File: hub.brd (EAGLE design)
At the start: 64.1 x 51.7 mm, 50 parts, among them IC1 SN65220DBV, IC2 SN65220DBV, IC3 SN65220DBV, IC4 SN65220DBV, IC5 SN65220DBV, U1 LM3526-L, X1 12MHz

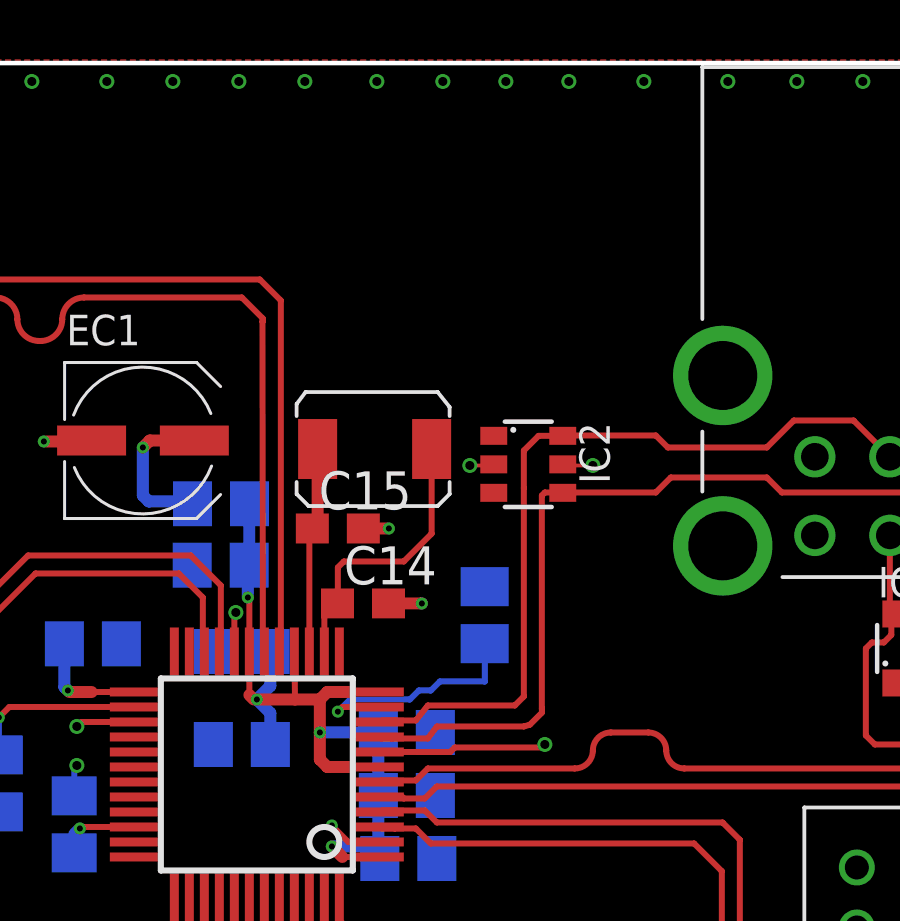
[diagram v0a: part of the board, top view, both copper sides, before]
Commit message: switch to crystal with correct drive level (supporting 600μW)
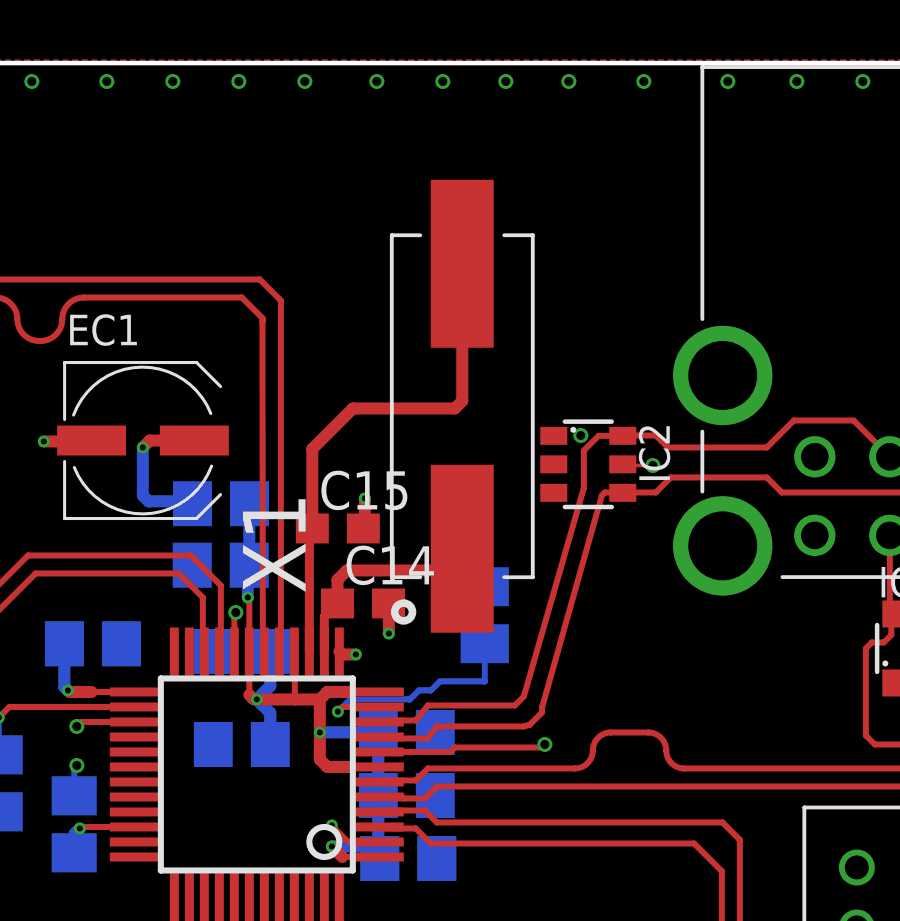
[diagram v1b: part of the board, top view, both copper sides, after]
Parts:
- X1: device Ava:ABRACON_ABM3_CRYSTAL -> ABLS-12.000MHZ-B2-T:XTAL_ABLS2-24.000MHZ-D4YF-T
- moved X1 4.62 mm to (39.0, 40.3), turned to 90 degrees
- moved IC2 2.00 mm to (43.2, 38.3)
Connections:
- net XIN: now also X1.1; no longer X1.P$1
- net XOUT: now also X1.2; no longer X1.P$2
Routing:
- net XOUT: track 6.86 -> 17.0 mm
- net XIN: track 9.40 -> 7.16 mm
- net D2_N: track 28.1 -> 26.4 mm
- net D2_P: track 27.5 -> 25.8 mm
- net GND: track 49.6 -> 49.5 mm, vias 122 -> 123

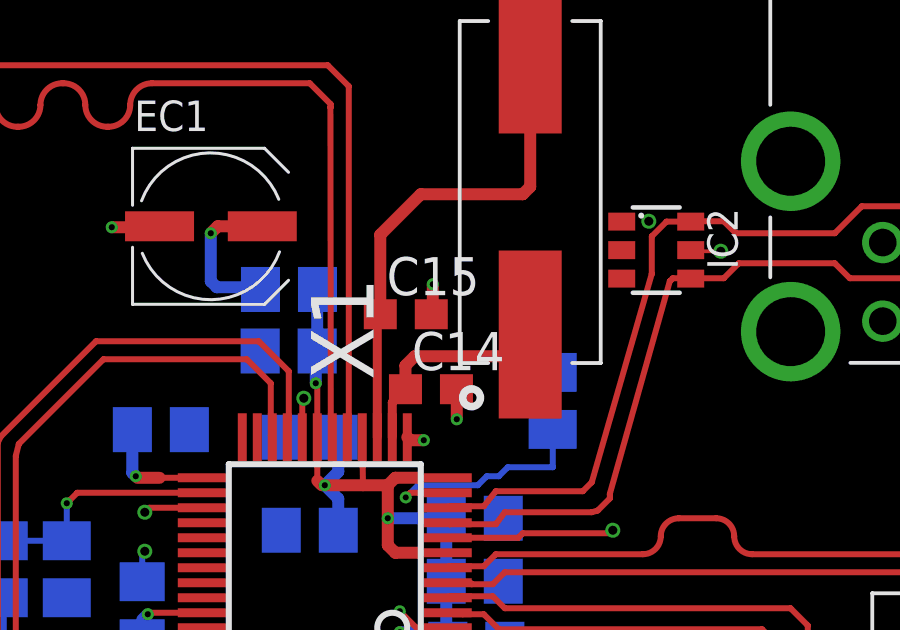
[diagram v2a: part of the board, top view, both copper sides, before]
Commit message: Switch to 0805 capacitors for consistency
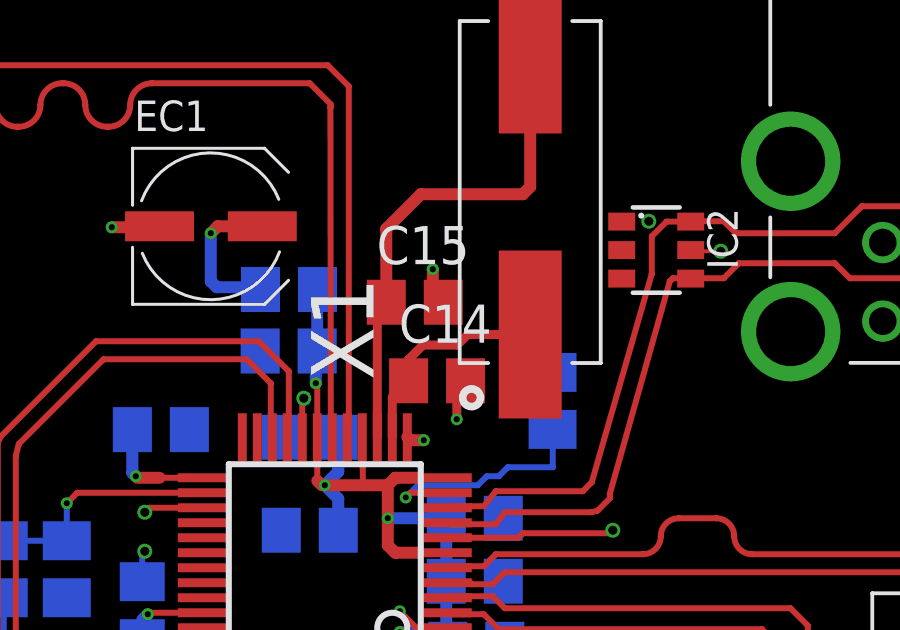
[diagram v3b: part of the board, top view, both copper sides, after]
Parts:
- C14, C15: device rcl:C0603 -> rcl:C0805
- moved C15 0.50 mm to (35.2, 36.6)
- moved C14 0.35 mm to (35.9, 34.0)
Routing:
- net GND: track 49.5 -> 50.1 mm
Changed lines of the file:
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@@
 <element name="R2" library="rcl" library_urn="urn:adsk.eagle:library:334" package="M0805" package3d_urn="urn:adsk.eagle:package:23556/1" value="100K" x="28.064" y="19.216" rot="MR0"/>
 <element name="R3" library="rcl" library_urn="urn:adsk.eagle:library:334" package="M0805" package3d_urn="urn:adsk.eagle:package:23556/1" value="650R 1%" x="39.794" y="33.31" rot="MR270"/>
-<element name="C14" library="rcl" library_urn="urn:adsk.eagle:library:334" package="C0603" package3d_urn="urn:adsk.eagle:package:23616/2" value="18P" x="35.739" y="33.702">
-<attribute name="DIGIKEY" value="1276-1089-1-ND" x="35.739" y="33.702" size="1.778" layer="27" display="off"/>
-<attribute name="OC_MOUSER" value="77-VJ0603A180JXACBC" x="35.739" y="33.702" size="1.778" layer="27" display="off"/>
-</element>
-<element name="C15" library="rcl" library_urn="urn:adsk.eagle:library:334" package="C0603" package3d_urn="urn:adsk.eagle:package:23616/2" value="18P" x="34.9" y="36.2">
-<attribute name="DIGIKEY" value="1276-1089-1-ND" x="34.9" y="36.2" size="1.778" layer="27" display="off"/>
-<attribute name="OC_MOUSER" value="77-VJ0603A180JXACBC" x="34.9" y="36.2" size="1.778" layer="27" display="off"/>
+<element name="C14" library="rcl" library_urn="urn:adsk.eagle:library:334" package="C0805" package3d_urn="urn:adsk.eagle:package:23617/2" value="18P" x="35.943" y="33.982">
+<attribute name="DIGIKEY" value="1276-1089-1-ND" x="35.943" y="33.982" size="1.778" layer="27" display="off"/>
+<attribute name="OC_MOUSER" value="77-VJ0603A180JXACBC" x="35.943" y="33.982" size="1.778" layer="27" display="off"/>
+</element>
+<element name="C15" library="rcl" library_urn="urn:adsk.eagle:library:334" package="C0805" package3d_urn="urn:adsk.eagle:package:23617/2" value="18P" x="35.2" y="36.6">
+<attribute name="DIGIKEY" value="1276-1089-1-ND" x="35.2" y="36.6" size="1.778" layer="27" display="off"/>
+<attribute name="OC_MOUSER" value="77-VJ0603A180JXACBC" x="35.2" y="36.6" size="1.778" layer="27" display="off"/>
 </element>
 <element name="X1" library="ABLS-12.000MHZ-B2-T" package="XTAL_ABLS2-24.000MHZ-D4YF-T" value="12MHz" x="39.048" y="40.274" rot="R90">
@@
 <wire x1="48.558" y1="14.741" x2="48.699" y2="14.6" width="0.4" layer="1"/>
 <wire x1="48.699" y1="14.6" x2="49.9" y2="14.6" width="0.4" layer="1"/>
-<via x="35.8" y="37.2" extent="1-16" drill="0.2"/>
+<via x="35.8" y="37.7" extent="1-16" drill="0.2"/>
 <via x="36.6" y="32.7" extent="1-16" drill="0.2"/>
 <via x="0.6" y="51.1" extent="1-16" drill="0.3"/>
@@
 <via x="1.9" y="0.6" extent="1-16" drill="0.3"/>
 <via x="0.6" y="0.6" extent="1-16" drill="0.3"/>
-<wire x1="35.8" y1="37.2" x2="35.8" y2="36.15" width="0.4" layer="1"/>
-<wire x1="35.8" y1="36.15" x2="35.75" y2="36.2" width="0.4" layer="1"/>
-<wire x1="36.6" y1="32.7" x2="36.6" y2="33.691" width="0.4" layer="1"/>
-<wire x1="36.6" y1="33.691" x2="36.589" y2="33.702" width="0.4" layer="1"/>
 <via x="35.5" y="32" extent="1-16" drill="0.2"/>
 <wire x1="35.5" y1="32" x2="35.05" y2="32" width="0.4" layer="1"/>
 <wire x1="35.05" y1="32" x2="34.95" y2="32.1" width="0.4" layer="1"/>
+<wire x1="36.893" y1="33.982" x2="36.6" y2="33.689" width="0.3" layer="1"/>
+<wire x1="36.6" y1="33.689" x2="36.6" y2="32.7" width="0.3" layer="1"/>
+<wire x1="36.15" y1="36.6" x2="35.8" y2="36.95" width="0.4" layer="1"/>
+<wire x1="35.8" y1="36.95" x2="35.8" y2="37.7" width="0.4" layer="1"/>
 </signal>
 <signal name="D0_N" class="1">
@@
 <contactref element="C14" pad="1"/>
 <contactref element="X1" pad="1"/>
-<wire x1="34.45" y1="32.1" x2="34.45" y2="33.263" width="0.3" layer="1"/>
-<wire x1="34.45" y1="33.263" x2="34.889" y2="33.702" width="0.3" layer="1"/>
-<wire x1="34.889" y1="33.702" x2="34.889" y2="34.489" width="0.4" layer="1"/>
-<wire x1="34.889" y1="34.489" x2="35.2" y2="34.8" width="0.4" layer="1"/>
-<wire x1="35.2" y1="34.8" x2="38.324" y2="34.8" width="0.4" layer="1"/>
-<wire x1="38.324" y1="34.8" x2="39.048" y2="35.524" width="0.4" layer="1"/>
+<wire x1="34.45" y1="32.1" x2="34.45" y2="33.439" width="0.3" layer="1"/>
+<wire x1="34.45" y1="33.439" x2="34.993" y2="33.982" width="0.3" layer="1"/>
+<wire x1="34.993" y1="33.982" x2="34.993" y2="34.693" width="0.3" layer="1"/>
+<wire x1="35.473" y1="35.173" x2="36.6147375" y2="35.173" width="0.3" layer="1"/>
+<wire x1="36.9657375" y1="35.524" x2="39.048" y2="35.524" width="0.3" layer="1"/>
+<wire x1="36.6147375" y1="35.173" x2="36.9657375" y2="35.524" width="0.3" layer="1"/>
+<wire x1="34.993" y1="34.693" x2="35.473" y2="35.173" width="0.3" layer="1"/>
 </signal>
 <signal name="XOUT">
@@
 <contactref element="C15" pad="1"/>
 <contactref element="X1" pad="2"/>
-<wire x1="33.95" y1="32.1" x2="33.95" y2="36.1" width="0.3" layer="1"/>
-<wire x1="33.95" y1="36.1" x2="34.05" y2="36.2" width="0.2" layer="1"/>
-<wire x1="34.05" y1="36.2" x2="34.05" y2="38.85" width="0.4" layer="1"/>
-<wire x1="35.4" y1="40.2" x2="38.8" y2="40.2" width="0.4" layer="1"/>
+<wire x1="38.8" y1="40.2" x2="35.4" y2="40.2" width="0.4" layer="1"/>
 <wire x1="38.8" y1="40.2" x2="39.048" y2="40.448" width="0.4" layer="1"/>
 <wire x1="39.048" y1="40.448" x2="39.048" y2="45.024" width="0.4" layer="1"/>
-<wire x1="34.05" y1="38.85" x2="35.4" y2="40.2" width="0.4" layer="1"/>
+<wire x1="33.95" y1="32.1" x2="33.95" y2="36.3" width="0.3" layer="1"/>
+<wire x1="34.25" y1="36.6" x2="33.95" y2="36.3" width="0.3" layer="1"/>
+<wire x1="35.4" y1="40.2" x2="34.25" y2="39.05" width="0.4" layer="1"/>
+<wire x1="34.25" y1="39.05" x2="34.25" y2="36.6" width="0.4" layer="1"/>
 </signal>
 <signal name="D3_N" class="1">

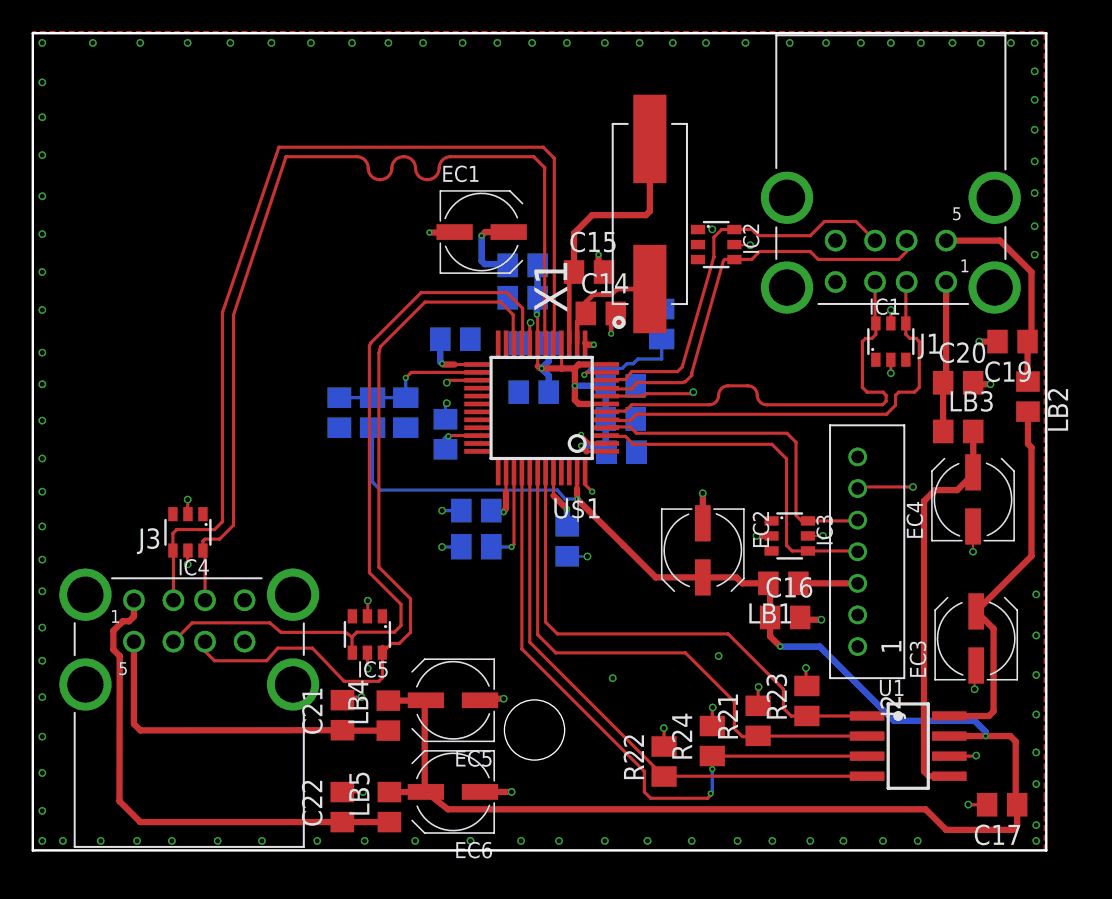
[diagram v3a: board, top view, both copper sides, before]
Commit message: Switch EC3, EC4, EC5, EC6 to ELXY250ELL121MF15D from vendor BOM
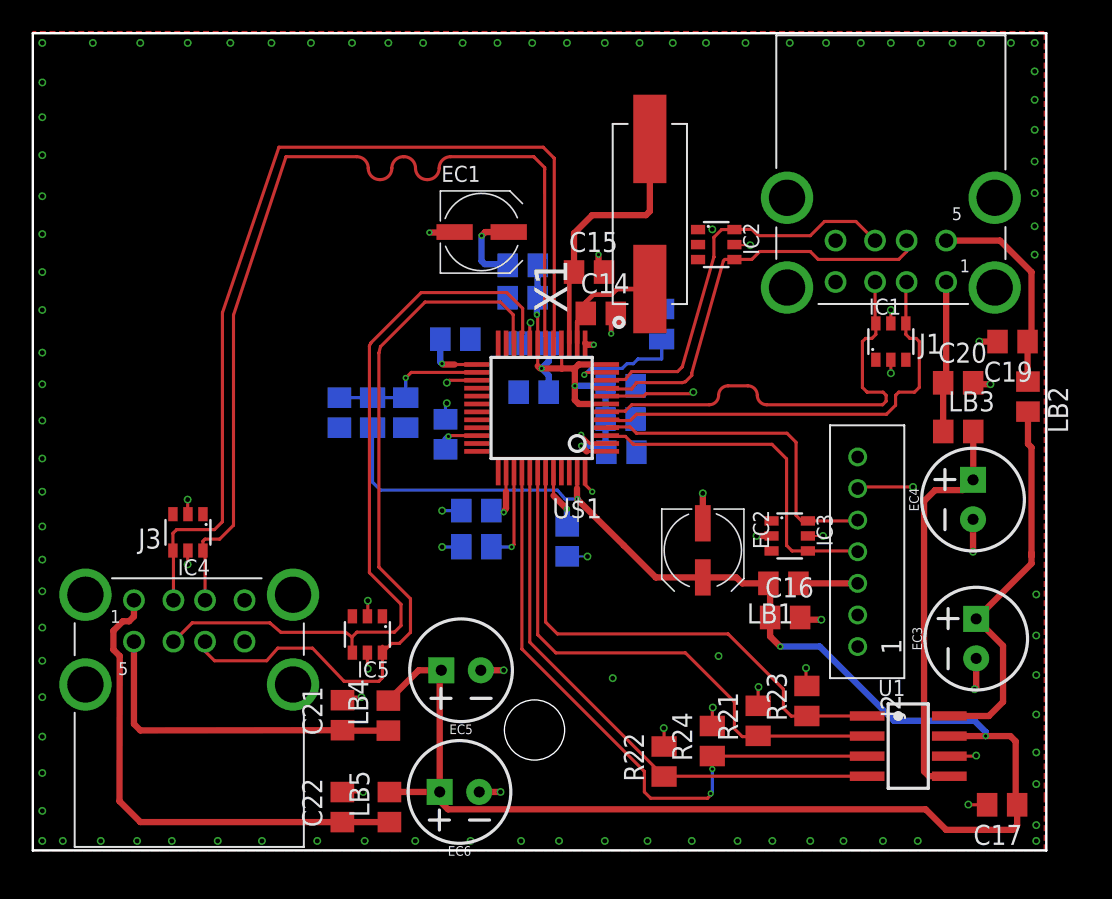
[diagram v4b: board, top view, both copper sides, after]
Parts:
- EC3, EC4, EC5, EC6: device rcl:UD-5X5,8_NICHICON -> SparkFun-Capacitors:CPOL-RADIAL-2.5MM-6.5MM
- moved EC5 1.96 mm to (27.1, 11.4)
- moved EC6 0.40 mm to (27.0, 3.70)
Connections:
- net GND: now also EC3.2, EC4.2, EC5.2, EC6.2; no longer EC3.-, EC4.-, EC5.-, EC6.-
- net PWR1: now also EC3.1; no longer EC3.+
- net PWR2: now also EC4.1; no longer EC4.+
- net VBUS: now also EC5.1, EC6.1; no longer EC5.+, EC6.+
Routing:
- net VBUS: track 113.1 -> 116.0 mm
- net PWR1: track 23.9 -> 24.6 mm

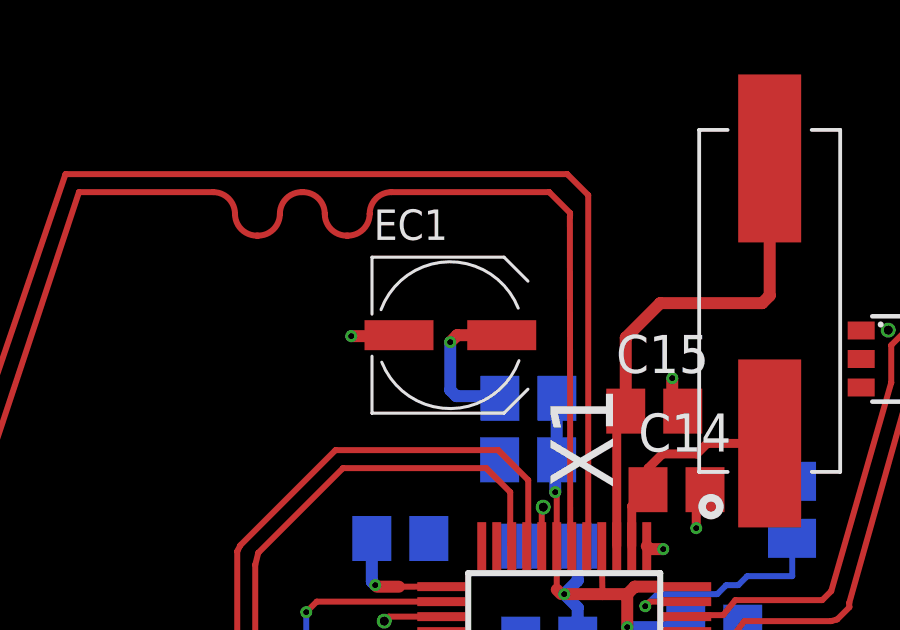
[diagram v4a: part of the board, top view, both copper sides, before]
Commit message: update EC1 with same footprint as EC3-EC6
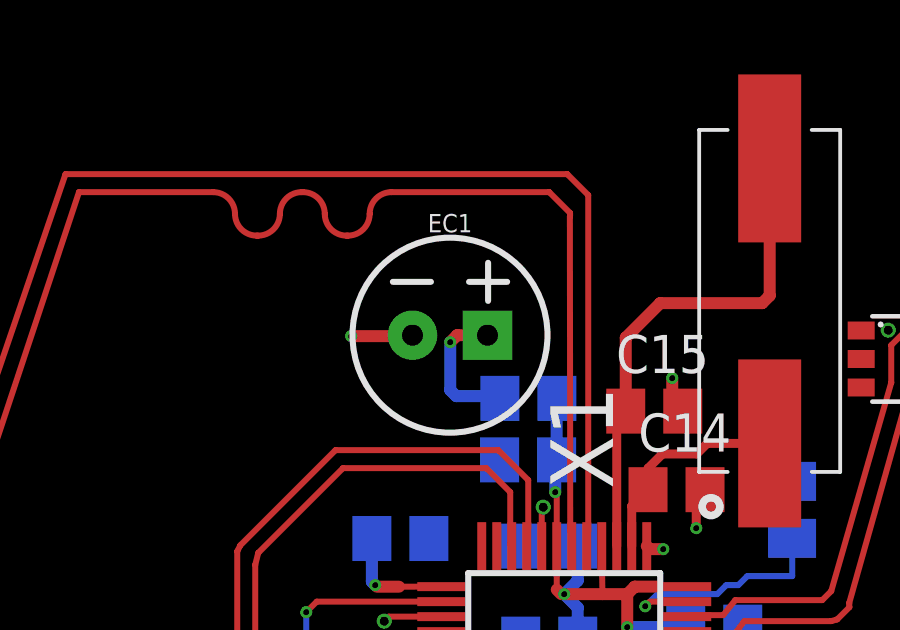
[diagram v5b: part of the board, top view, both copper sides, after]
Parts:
- EC1: device rcl:UD-5X5,8_NICHICON -> SparkFun-Capacitors:CPOL-RADIAL-2.5MM-6.5MM
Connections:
- net +3V3: now also EC1.1; no longer EC1.+
- net GND: now also EC1.2; no longer EC1.-
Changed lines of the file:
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@@
 <element name="IC2" library="sn65220_40" package="SOT23-6" value="SN65220DBV" x="43.248" y="38.338" rot="R270"/>
 <element name="C1" library="rcl" library_urn="urn:adsk.eagle:library:334" package="C0805" package3d_urn="urn:adsk.eagle:package:23617/2" value="0.1uF" x="30.996" y="34.976" rot="MR0"/>
-<element name="EC1" library="rcl" library_urn="urn:adsk.eagle:library:334" package="UD-5X5,8_NICHICON" package3d_urn="urn:adsk.eagle:package:23470/1" value="10uF" x="28.392" y="39.132">
-<attribute name="DIGIKEY" value="PCE3878CT-ND" x="28.392" y="39.132" size="1.778" layer="27" display="off"/>
-<attribute name="MPN" value="EEE-1CA100SR" x="28.392" y="39.132" size="1.778" layer="27" display="off"/>
-<attribute name="OC_MOUSER" value="667-EEE-1CA100SR" x="28.392" y="39.132" size="1.778" layer="27" display="off"/>
+<element name="EC1" library="SparkFun-Capacitors" library_urn="urn:adsk.eagle:library:510" package="CPOL-RADIAL-2.5MM-6.5MM" package3d_urn="urn:adsk.eagle:package:37415/1" value="10uF" x="28.392" y="39.132">
+<attribute name="DIGIKEY" value="493-16013-1-ND" x="28.392" y="39.132" size="1.778" layer="27" display="off"/>
+<attribute name="MF" value="nichicon" x="28.392" y="39.132" size="1.778" layer="27" display="off"/>
+<attribute name="MPN" value="UST1H100MDD1TE" x="28.392" y="39.132" size="1.778" layer="27" display="off"/>
+<attribute name="OC_MOUSER" value="647-UST1H100MDD1TE" x="28.392" y="39.132" size="1.778" layer="27" display="off"/>
+<attribute name="PROD_ID" value="CAP-08439" x="28.392" y="39.132" size="1.778" layer="27" display="off"/>
+<attribute name="VALUE" value="100uF" x="28.392" y="39.132" size="1.778" layer="27" display="off"/>
 </element>
 <element name="C2" library="rcl" library_urn="urn:adsk.eagle:library:334" package="C0805" package3d_urn="urn:adsk.eagle:package:23617/2" value="1uF" x="31.7" y="32.1" rot="MR0"/>
@@
 <contactref element="IC2" pad="5"/>
 <contactref element="IC2" pad="2"/>
-<contactref element="EC1" pad="-"/>
+<contactref element="EC1" pad="2"/>
 <contactref element="C1" pad="2"/>
 <contactref element="C2" pad="2"/>
@@
 <via x="0.6" y="4.9" extent="1-16" drill="0.3"/>
 <via x="0.6" y="2.5" extent="1-16" drill="0.3"/>
-<wire x1="26.692" y1="39.132" x2="26.66" y2="39.1" width="0.4" layer="1"/>
+<wire x1="27.142" y1="39.132" x2="26.66" y2="39.1" width="0.4" layer="1"/>
 <wire x1="26.66" y1="39.1" x2="25.1" y2="39.1" width="0.4" layer="1"/>
 <via x="25.1" y="39.1" extent="1-16" drill="0.2"/>
@@
 </signal>
 <signal name="+3V3">
-<contactref element="EC1" pad="+"/>
+<contactref element="EC1" pad="1"/>
 <contactref element="U$1" pad="48"/>
 <contactref element="R21" pad="2"/>
@@
 <wire x1="26.3" y1="26.2" x2="26.114" y2="26.014" width="0.4" layer="16"/>
 <wire x1="26.114" y1="26.014" x2="26.114" y2="25.386" width="0.2" layer="16"/>
-<wire x1="30.117" y1="39.132" x2="28.632" y2="39.132" width="0.4" layer="1"/>
+<wire x1="29.642" y1="39.132" x2="28.632" y2="39.132" width="0.4" layer="1"/>
 <wire x1="28.632" y1="39.132" x2="28.4" y2="38.9" width="0.4" layer="1"/>
 <via x="28.4" y="38.9" extent="1-16" drill="0.2"/>
